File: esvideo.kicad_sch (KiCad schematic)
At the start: 29 parts, among them U8 BT253, U9 BT473

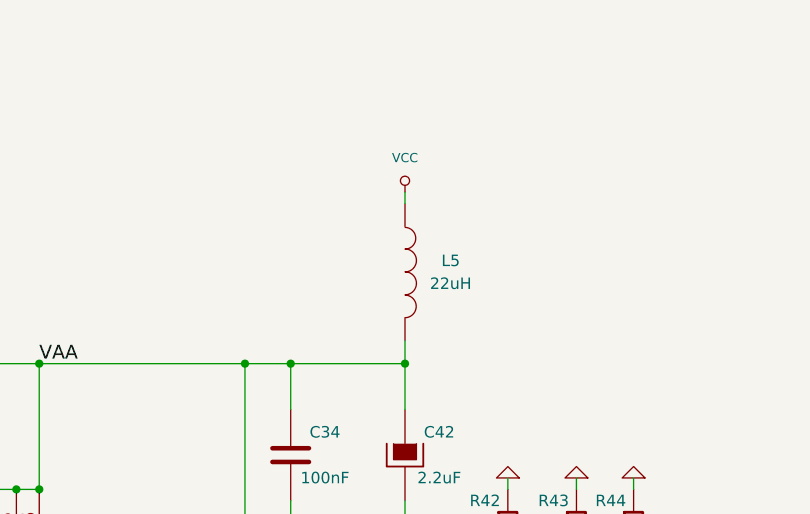
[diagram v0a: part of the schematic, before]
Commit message: update to kicad 9
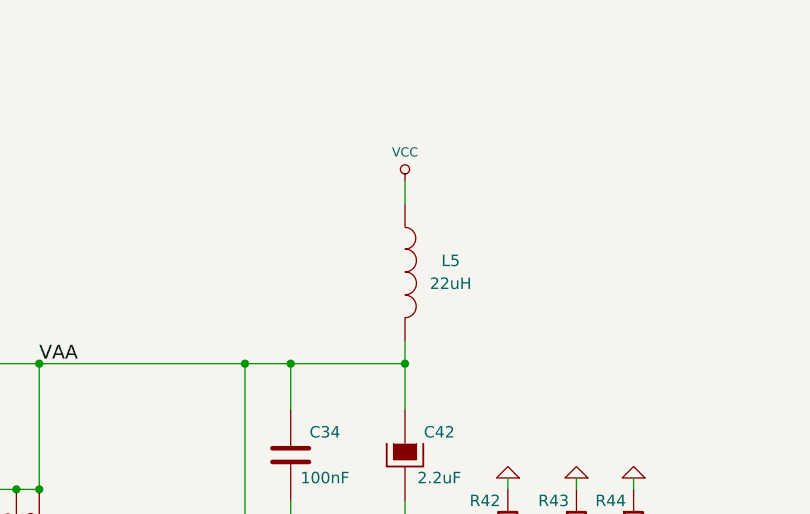
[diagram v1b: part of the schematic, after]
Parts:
- C32, C33, C34, C35, C36, C37, C52, R15, R22, R23, R24, R36, R37, R38, R42, R43, R44, R45, R46, R47, R8: footprint Resistor_SMD:R_1206_3216Metric_Pad1.24x1.80mm_HandSolder -> Resistor_SMD:R_1206_3216Metric_Pad1.30x1.75mm_HandSolder
- C39, C40, C41, C42, C51: footprint Resistor_SMD:R_1210_3225Metric_Pad1.24x2.70mm_HandSolder -> Resistor_SMD:R_1210_3225Metric_Pad1.30x2.65mm_HandSolder
- L5: footprint Resistor_SMD:R_1812_4532Metric_Pad1.24x3.50mm_HandSolder -> Resistor_SMD:R_1812_4532Metric_Pad1.30x3.40mm_HandSolder
